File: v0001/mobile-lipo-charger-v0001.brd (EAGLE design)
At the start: 82.9 x 96.2 mm, 76 parts, among them IC1 AD8610MR, IC3 AD8610MR, IC5 STM32F429NGH, SW2 DHT-4235A, U3 3.3V, U4 3.3V

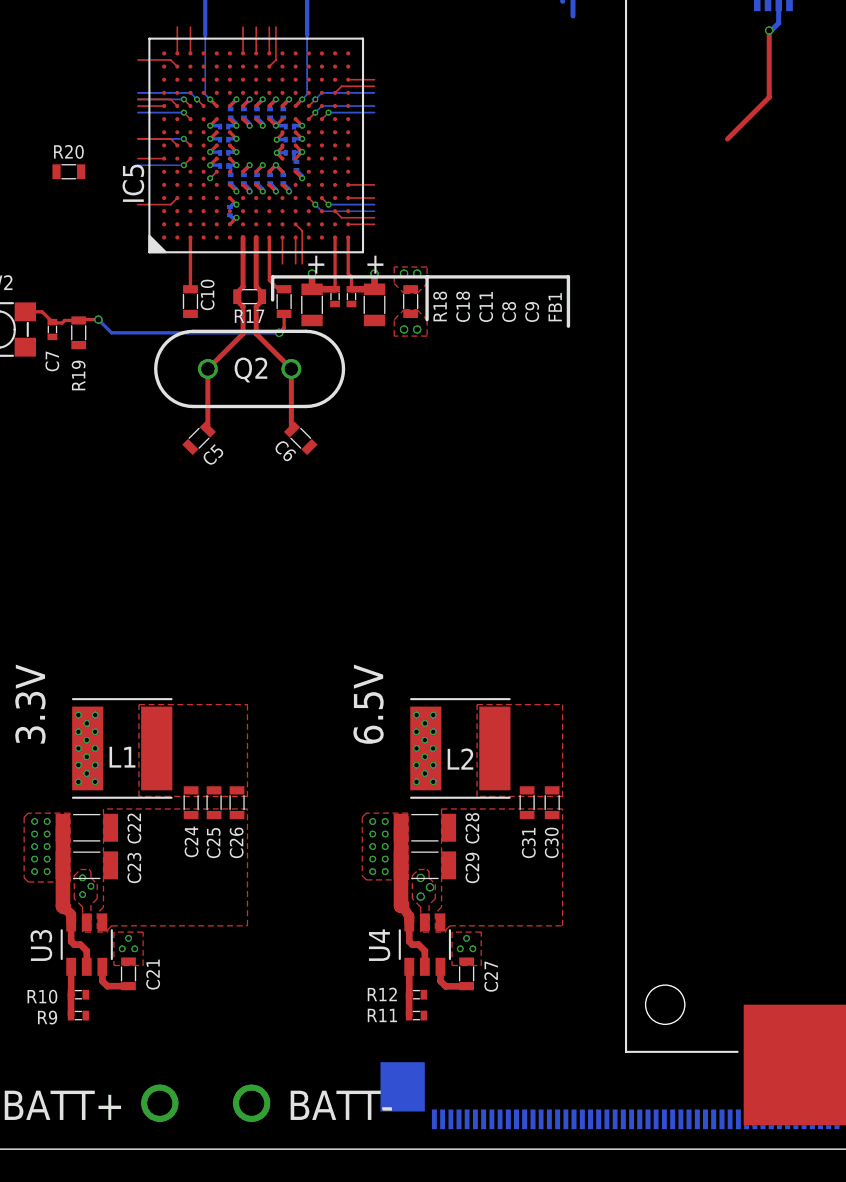
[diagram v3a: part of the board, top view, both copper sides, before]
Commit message: Routing
Routed some signals for the TFT
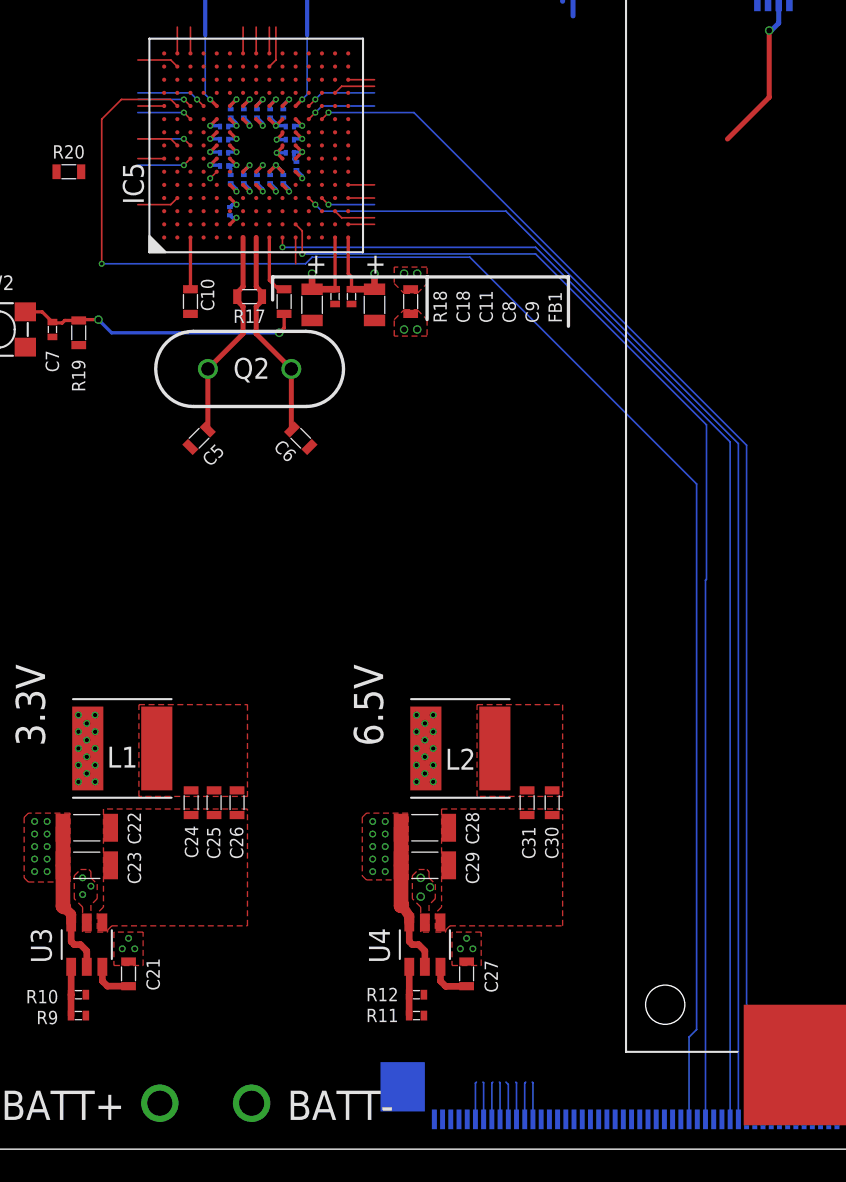
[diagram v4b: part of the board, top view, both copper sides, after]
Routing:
- net B2: track 2.57 -> 95.0 mm, vias 0 -> 1
- net DCX_SCL: track 1.60 -> 73.8 mm, vias 0 -> 1
- net TE: track 3.37 -> 75.4 mm
- net SDA: track 2.57 -> 73.2 mm, vias 0 -> 1
- net CSX: track 4.33 -> 73.5 mm
- net RST: track 0.00 -> 2.32 mm
- net IM0: track 0.00 -> 2.29 mm
- net HSYNC: track 1.60 -> 3.89 mm
- net IM2: track 3.37 -> 5.66 mm
- net VSYNC: track 3.37 -> 5.65 mm
- net IM3: track 1.60 -> 3.88 mm
- net IM1: track 4.33 -> 6.61 mm
- net DOTCLK: track 2.57 -> 4.85 mm
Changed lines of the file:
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@@
 <contactref element="JP2" pad="10"/>
 <contactref element="J1" pad="10"/>
-<wire x1="34.541" y1="12.735" x2="12.28" y2="105.27" width="0" layer="19" extent="16-16"/>
+<wire x1="34.541" y1="12.735" x2="34.541" y2="14.859" width="0.1016" layer="16"/>
+<wire x1="34.541" y1="14.859" x2="34.4" y2="15" width="0.1016" layer="16"/>
+<wire x1="34.4" y1="15" x2="12.28" y2="105.27" width="0" layer="19" extent="16-16"/>
 </signal>
 <signal name="RST_BUTTON">
@@
 <contactref element="J1" pad="32"/>
 <wire x1="14.4" y1="74.4" x2="14" y2="74.8" width="0.1016" layer="1"/>
-<wire x1="14" y1="74.8" x2="12" y2="74.8" width="0.1016" layer="1"/>
-<wire x1="45.541" y1="12.735" x2="14.4" y2="74.4" width="0" layer="19" extent="1-16"/>
+<wire x1="45.541" y1="12.735" x2="45.541" y2="17.741" width="0.1016" layer="16"/>
+<wire x1="45.541" y1="17.741" x2="46" y2="18.2" width="0.1016" layer="16"/>
+<wire x1="46" y1="51.4" x2="46" y2="18.2" width="0.1016" layer="16"/>
+<via x="9.8" y="64.8" extent="1-16" drill="0.2032"/>
+<wire x1="9.8" y1="64.8" x2="22.2" y2="64.8" width="0.1016" layer="16"/>
+<wire x1="22.2" y1="64.8" x2="22.6" y2="65.2" width="0.1016" layer="16"/>
+<wire x1="22.6" y1="65.2" x2="32.2" y2="65.2" width="0.1016" layer="16"/>
+<wire x1="14" y1="74.8" x2="11" y2="74.8" width="0.1016" layer="1"/>
+<wire x1="11" y1="74.8" x2="9.8" y2="73.6" width="0.1016" layer="1"/>
+<wire x1="9.8" y1="73.6" x2="9.8" y2="64.8" width="0.1016" layer="1"/>
+<wire x1="32.2" y1="65.2" x2="46" y2="51.4" width="0.1016" layer="16"/>
 </signal>
 <signal name="B3">
@@
 <wire x1="23.2" y1="68.8" x2="23.6" y2="68.4" width="0.1016" layer="1"/>
 <wire x1="23.6" y1="68.4" x2="26.4" y2="68.4" width="0.1016" layer="16"/>
-<wire x1="35.041" y1="12.735" x2="26.4" y2="68.4" width="0" layer="19" extent="16-16"/>
+<wire x1="35.041" y1="12.735" x2="35.041" y2="14.959" width="0.1016" layer="16"/>
+<wire x1="35.041" y1="14.959" x2="35" y2="15" width="0.1016" layer="16"/>
+<wire x1="35.041" y1="14.959" x2="26.4" y2="68.4" width="0" layer="19" extent="16-16"/>
 </signal>
 <signal name="HSYNC">
@@
 <contactref element="J1" pad="12"/>
 <wire x1="19.2" y1="77.6" x2="19.2" y2="79.2" width="0.1016" layer="1"/>
-<wire x1="35.541" y1="12.735" x2="19.2" y2="77.6" width="0" layer="19" extent="1-16"/>
+<wire x1="35.541" y1="12.735" x2="35.541" y2="14.941" width="0.1016" layer="16"/>
+<wire x1="35.541" y1="14.941" x2="35.6" y2="15" width="0.1016" layer="16"/>
+<wire x1="35.6" y1="15" x2="19.2" y2="77.6" width="0" layer="19" extent="1-16"/>
 </signal>
 <signal name="TE">
@@
 <via x="23.6" y="74" extent="1-16" drill="0.2032"/>
 <wire x1="23.2" y1="73.6" x2="23.6" y2="74" width="0.1016" layer="1"/>
-<wire x1="23.6" y1="74" x2="26.4" y2="74" width="0.1016" layer="16"/>
-<wire x1="49.041" y1="12.735" x2="26.4" y2="74" width="0" layer="19" extent="16-16"/>
+<wire x1="49.041" y1="12.735" x2="49.041" y2="53.759" width="0.1016" layer="16"/>
+<wire x1="49.041" y1="53.759" x2="28.8" y2="74" width="0.1016" layer="16"/>
+<wire x1="28.8" y1="74" x2="23.6" y2="74" width="0.1016" layer="16"/>
 </signal>
 <signal name="DOTCLK">
@@
 <wire x1="20" y1="76.8" x2="20.4" y2="77.2" width="0.1016" layer="1"/>
 <wire x1="20.4" y1="77.2" x2="20.4" y2="79.2" width="0.1016" layer="1"/>
-<wire x1="36.041" y1="12.735" x2="20" y2="76.8" width="0" layer="19" extent="1-16"/>
+<wire x1="36.041" y1="12.735" x2="36.041" y2="14.959" width="0.1016" layer="16"/>
+<wire x1="36.041" y1="14.959" x2="36" y2="15" width="0.1016" layer="16"/>
+<wire x1="36" y1="15" x2="20" y2="76.8" width="0" layer="19" extent="1-16"/>
 </signal>
 <signal name="ENABLE">
@@
 <wire x1="22.4" y1="68.8" x2="22.8" y2="68.4" width="0.1016" layer="1"/>
 <wire x1="22.8" y1="68.4" x2="23.2" y2="68" width="0.1016" layer="16"/>
-<wire x1="23.2" y1="68" x2="26.4" y2="68" width="0.1016" layer="16"/>
-<wire x1="48.541" y1="12.735" x2="26.4" y2="68" width="0" layer="19" extent="16-16"/>
+<wire x1="48.541" y1="12.735" x2="48.541" y2="53.859" width="0.1016" layer="16"/>
+<wire x1="23.2" y1="68" x2="34.4" y2="68" width="0.1016" layer="16"/>
+<wire x1="34.4" y1="68" x2="48.541" y2="53.859" width="0.1016" layer="16"/>
 </signal>
 <signal name="RDX">
@@
 <contactref element="IC5" pad="K1"/>
 <contactref element="J1" pad="37"/>
-<wire x1="20.8" y1="66.4" x2="20.8" y2="64.8" width="0.1016" layer="1"/>
-<wire x1="48.041" y1="12.735" x2="20.8" y2="64.8" width="0" layer="19" extent="1-16"/>
+<wire x1="20.8" y1="66.4" x2="20.8" y2="66" width="0.1016" layer="1"/>
+<wire x1="48.041" y1="53.959" x2="48.041" y2="12.735" width="0.1016" layer="16"/>
+<via x="20.8" y="65.8" extent="1-16" drill="0.2032"/>
+<wire x1="20.8" y1="65.8" x2="36.2" y2="65.8" width="0.1016" layer="16"/>
+<wire x1="36.2" y1="65.8" x2="48.041" y2="53.959" width="0.1016" layer="16"/>
+<wire x1="20.8" y1="65.8" x2="20.8" y2="66" width="0" layer="19" extent="1-1"/>
 </signal>
 <signal name="SDA">
@@
 <contactref element="J1" pad="34"/>
 <wire x1="21.6" y1="67.2" x2="22" y2="66.8" width="0.1016" layer="1"/>
-<wire x1="22" y1="66.8" x2="22" y2="64.8" width="0.1016" layer="1"/>
-<wire x1="46.541" y1="12.735" x2="22" y2="64.8" width="0" layer="19" extent="1-16"/>
+<wire x1="46.541" y1="12.735" x2="46.541" y2="45.541" width="0.1016" layer="16"/>
+<wire x1="46.541" y1="45.541" x2="46.6" y2="45.6" width="0.1016" layer="16"/>
+<via x="22" y="65.4" extent="1-16" drill="0.2032"/>
+<wire x1="22" y1="66.8" x2="22" y2="65.4" width="0.1016" layer="1"/>
+<wire x1="46.6" y1="55" x2="46.6" y2="45.6" width="0.1016" layer="16"/>
+<wire x1="22" y1="65.4" x2="36.2" y2="65.4" width="0.1016" layer="16"/>
+<wire x1="36.2" y1="65.4" x2="46.6" y2="55" width="0.1016" layer="16"/>
 </signal>
 <signal name="IM0">
 <contactref element="IC5" pad="D12"/>
 <contactref element="J1" pad="6"/>
-<wire x1="32.541" y1="12.735" x2="16" y2="75.2" width="0" layer="19" extent="1-16"/>
+<wire x1="32.541" y1="12.735" x2="32.541" y2="14.941" width="0.1016" layer="16"/>
+<wire x1="32.541" y1="14.941" x2="32.6" y2="15" width="0.1016" layer="16"/>
+<wire x1="32.6" y1="15" x2="16" y2="75.2" width="0" layer="19" extent="1-16"/>
 </signal>
 <signal name="IM1">
@@
 <wire x1="15.6" y1="74.8" x2="15.2" y2="75.2" width="0.1016" layer="16"/>
 <wire x1="15.2" y1="75.2" x2="12" y2="75.2" width="0.1016" layer="16"/>
-<wire x1="33.041" y1="12.735" x2="16" y2="74.4" width="0" layer="19" extent="1-16"/>
+<wire x1="33.041" y1="12.735" x2="33.041" y2="14.959" width="0.1016" layer="16"/>
+<wire x1="33.041" y1="14.959" x2="33" y2="15" width="0.1016" layer="16"/>
+<wire x1="33" y1="15" x2="16" y2="74.4" width="0" layer="19" extent="1-16"/>
 </signal>
 <signal name="IM2">
@@
 <wire x1="15.2" y1="73.6" x2="14.8" y2="74" width="0.1016" layer="1"/>
 <wire x1="14.8" y1="74" x2="12" y2="74" width="0.1016" layer="16"/>
-<wire x1="33.541" y1="12.735" x2="15.2" y2="73.6" width="0" layer="19" extent="1-16"/>
+<wire x1="33.541" y1="12.735" x2="33.541" y2="14.941" width="0.1016" layer="16"/>
+<wire x1="33.541" y1="14.941" x2="33.6" y2="15" width="0.1016" layer="16"/>
+<wire x1="33.6" y1="15" x2="15.2" y2="73.6" width="0" layer="19" extent="1-16"/>
 </signal>
 <signal name="IM3">
@@
 <contactref element="J1" pad="9"/>
 <wire x1="13.6" y1="74.4" x2="12" y2="74.4" width="0.1016" layer="1"/>
-<wire x1="34.041" y1="12.735" x2="13.6" y2="74.4" width="0" layer="19" extent="1-16"/>
+<wire x1="34.041" y1="12.735" x2="34.041" y2="14.959" width="0.1016" layer="16"/>
+<wire x1="34.041" y1="14.959" x2="34" y2="15" width="0.1016" layer="16"/>
+<wire x1="34" y1="15" x2="13.6" y2="74.4" width="0" layer="19" extent="1-16"/>
 </signal>
 </signals>

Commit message: LED Backlight
Added the LCD backlight control and PSU
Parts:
- added R1: 1k, common:0603L3
- added R2: 10k, common:0603L3
- added R3: 12R, common:0603L3
- added T1, T2, T3: BC846, transistor:SOT23
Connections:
- removed net TFT_IOVCC: J1.40, J1.41
- removed net TFT_LED_A: J1.2, J1.3, J1.4, J1.48, J1.49, J1.5
- removed net TFT_SDO: J1.33
- removed net TFT_VCI: J1.42
- new net DB0: J1.32
- new net DB1: J1.31
- new net DB10: J1.22
- new net DB11: J1.21
- new net DB12: J1.20
- new net DB13: J1.19
- new net DB14: J1.18
- new net DB15: J1.17
- new net DB16: J1.16
- new net DB17: J1.15
- new net DB2: J1.30
- new net DB3: J1.29
- new net DB4: J1.28
- new net DB5: J1.27
- new net DB6: J1.26
- new net DB7: J1.25
- new net LCD_BLED: R1.P$1
- new net N$5: T2.2, T3.1, T3.3
- new net N$6: R3.P$2, T1.2
- new net N$7: R1.P$2, R2.P$1, T1.1, T2.1, T2.3
- new net VCC_BLED: J1.2, J1.3, J1.4, J1.5
- net B2: no longer J1.32
- net B3: no longer J1.31
- net B4: no longer J1.30
- net B5: no longer J1.29
- net B6: no longer J1.28
- net B7: no longer J1.27
- net DOTCLK: no longer J1.13
- net G2: no longer J1.26
- net G3: no longer J1.25
- net G4: no longer J1.24
- net G5: no longer J1.23
- net G6: no longer J1.22
- net G7: no longer J1.21
- net GND: now also J1.23, J1.24, J1.34, J1.48, J1.49, J1.6, J1.7, J1.8, R3.P$1, T3.2
- net HSYNC: no longer J1.12
- net IM0: no longer J1.6
- net IM1: no longer J1.7
- net IM2: no longer J1.8
- net IM3: no longer J1.9
- net R2: no longer J1.20
- net R3: no longer J1.19
- net R4: no longer J1.18
- net R5: no longer J1.17
- net R6: no longer J1.16
- net R7: no longer J1.15
- net SDA: no longer J1.34
- net TE: no longer J1.39
- net TFT_LED_K: now also T1.3
- net VDD: now also J1.40, J1.41, J1.42, J1.9, R2.P$2
- net VSYNC: no longer J1.11
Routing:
- net R3: track 1.60 -> 78.7 mm, vias 0 -> 3
- net G2: track 2.57 -> 65.4 mm, vias 0 -> 1
- net B5: track 1.60 -> 62.9 mm, vias 0 -> 1
- net SDA: track 73.2 -> 40.3 mm
- net TE: track 75.4 -> 58.6 mm
- net B2: track 95.0 -> 90.1 mm
- net IM0: track 2.29 -> 0.00 mm
- net HSYNC: track 3.89 -> 1.60 mm
- net IM2: track 5.66 -> 3.37 mm
- net VSYNC: track 5.65 -> 3.37 mm
- net IM3: track 3.88 -> 1.60 mm
- net IM1: track 6.61 -> 4.33 mm
- net DOTCLK: track 4.85 -> 2.57 mm
- net VDD: track 29.3 -> 30.1 mm
- net GND: track 20.7 -> 21.3 mm
- added copper zone on layer 16, net N$5
- added copper zone on layer 16, net N$6
- added copper zone on layer 16, net N$7
- added copper zone on layer 16, net TFT_LED_K

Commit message: TFT Changes
Changed the data lines to the TFT and rerouted some of the charge IC lines
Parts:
- moved JP2 5.56 mm to (4.40, 99.2), turned to 270 degrees
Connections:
- removed net B2: IC5.B11
- removed net B3: IC5.B8
- removed net B4: IC5.C7
- removed net B5: IC5.R2
- removed net B6: IC5.A7
- removed net B7: IC5.B4
- removed net CSX: IC5.M4, J1.38
- removed net DCX_SCL: IC5.K1, J1.37
- removed net DOTCLK: IC5.J14
- removed net G2: IC5.P3
- removed net G3: IC5.C8
- removed net G4: IC5.P12
- removed net G5: IC5.R13
- removed net G6: IC5.G15
- removed net G7: IC5.C11
- removed net HSYNC: IC5.H15
- removed net IM0: IC5.D12
- removed net IM1: IC5.D11
- removed net IM2: IC5.C10
- removed net IM3: IC5.A11
- removed net N$3: IC5.J1, R18.P$2
- removed net R2: IC5.B14
- removed net R3: IC5.R5
- removed net R4: IC5.C15
- removed net R5: IC5.B15
- removed net R6: IC5.R4
- removed net R7: IC5.J15
- removed net RDX: IC5.M10
- removed net SDA: IC5.L2
- removed net TE: IC5.N10
- removed net TFT_RD#: J1.35
- removed net TFT_WR_RS#: J1.36
- removed net VSYNC: IC5.N4
- removed net WRX_DCX: IC5.M11
- new net LCD_CS: IC5.A11, J1.38
- new net LCD_DC: IC5.D2, J1.37
- new net LCD_RD: IC5.D11, J1.35
- new net LCD_WR: IC5.C10, J1.36
- new net N$12: IC5.R15
- new net NRST: IC5.J1, JP2.10, R18.P$2
- new net TDI: IC5.A13, JP2.8
- new net TDO: IC5.A10, JP2.6
- new net TRST: IC5.A9, JP2.7
- net BATT1_CE: now also IC5.P14
- net BATT1_CHARGE: now also IC5.N14
- net BATT1_DONE: now also IC5.N15
- net BATT2_CE: now also IC5.P15
- net BATT2_CHARGE: now also IC5.M14
- net BATT2_DONE: now also IC5.M15
- net DB0: now also IC5.L12
- net DB1: now also IC5.K13
- net DB10: now also IC5.P10
- net DB11: now also IC5.R10
- net DB12: now also IC5.R12
- net DB13: now also IC5.P11
- net DB14: now also IC5.R11
- net DB15: now also IC5.L15
- net DB16: now also IC5.L14
- net DB17: now also IC5.K15
- net DB2: now also IC5.B12
- net DB3: now also IC5.C12
- net DB4: now also IC5.R8
- net DB5: now also IC5.N9
- net DB6: now also IC5.P9
- net DB7: now also IC5.R9
- net ENABLE: no longer IC5.L1
- net GND: now also J1.11, J1.12, J1.13
- net RST: no longer JP2.10
- net TCK_SWCLK: now also IC5.A14
- net TMS_SWDIO: now also IC5.A15
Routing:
- net B2: track 90.1 -> 0.00 mm, vias 1 -> 0
- net R3: track 78.7 -> 0.00 mm, vias 3 -> 0
- net DCX_SCL: track 73.6 -> 0.00 mm, vias 1 -> 0
- net CSX: track 73.3 -> 0.00 mm, vias 1 -> 0
- net LCD_DC: track 0.00 -> 73.2 mm, vias 0 -> 1
- net LCD_CS: track 0.00 -> 72.7 mm, vias 0 -> 1
- net G2: track 65.4 -> 0.00 mm, vias 1 -> 0
- net B5: track 62.9 -> 0.00 mm, vias 1 -> 0
- net TE: track 58.6 -> 0.00 mm, vias 1 -> 0
- net SDA: track 40.3 -> 0.00 mm, vias 1 -> 0
- net TDO: track 0.00 -> 33.9 mm
- net TMS_SWDIO: track 0.00 -> 32.1 mm
- net TRST: track 0.00 -> 31.6 mm
- net TCK_SWCLK: track 0.00 -> 31.4 mm
- net TDI: track 0.00 -> 26.9 mm
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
